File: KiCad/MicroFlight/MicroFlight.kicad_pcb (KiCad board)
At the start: 2 copper layers, 38 x 17 mm, 65 parts, among them J1 C2CK, J10 SRV3, J2 C2D, J3 A, J4 B, J5 C, J6 BIND, J7 BAT, J8 SRV1, J9 SRV2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

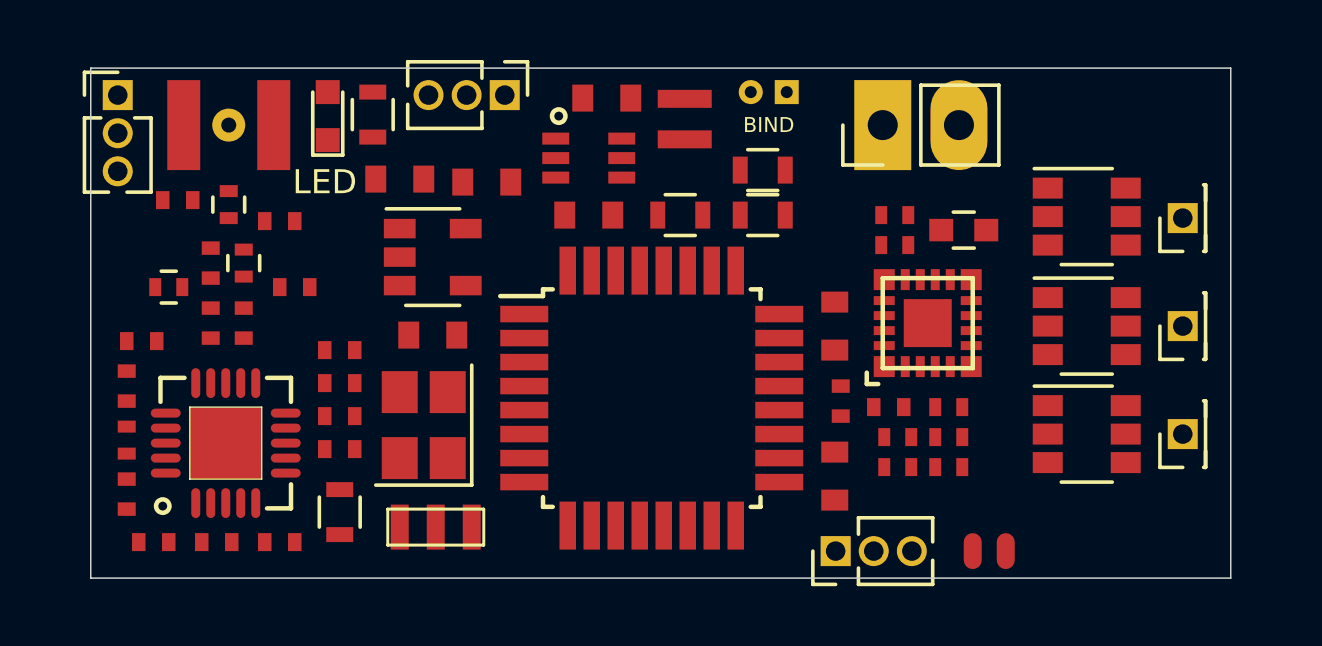
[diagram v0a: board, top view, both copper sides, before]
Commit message: PCB - added optional shunt for current sensing
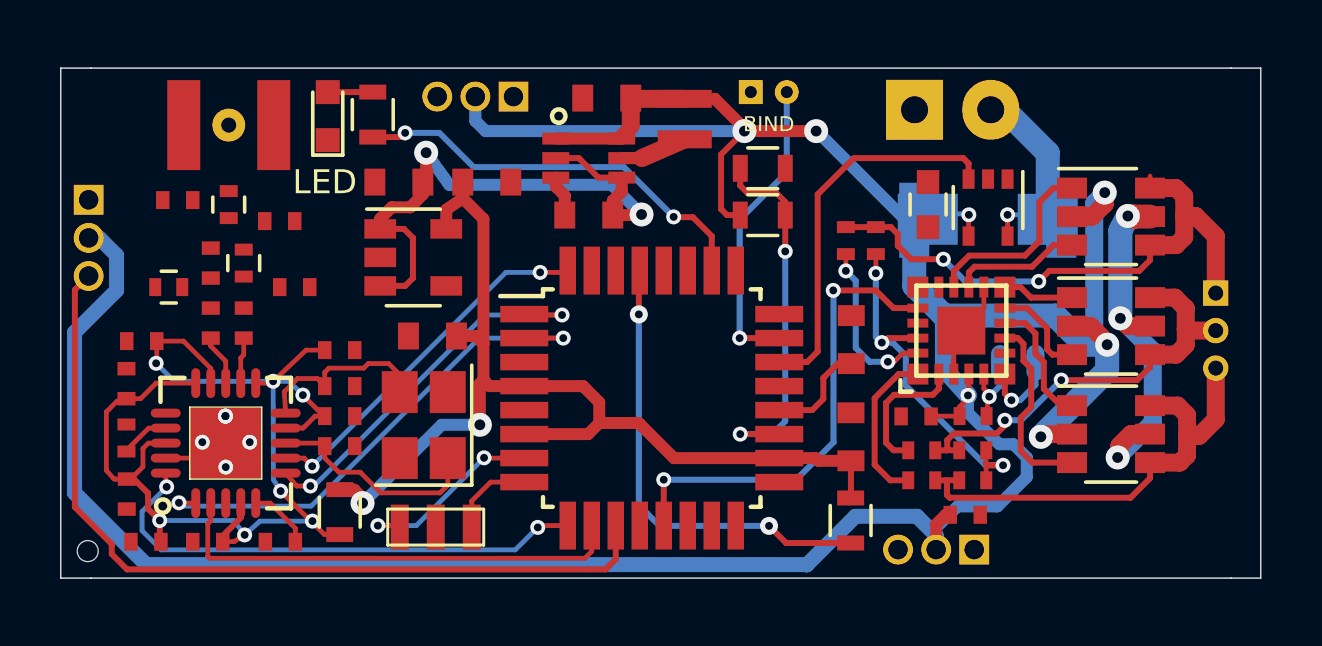
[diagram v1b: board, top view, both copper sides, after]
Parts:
- removed J4: B, Pin_Headers:Pin_Header_Straight_1x01_Pitch1.27mm
- removed J5: C, Pin_Headers:Pin_Header_Straight_1x01_Pitch1.27mm
- added R13: 0.022, Resistors_SMD:R_1206_HandSoldering, B.Cu at (126.9, 85.5)
- added R14: 0.022, Resistors_SMD:R_2010, B.Cu at (126.9, 85.6)
- added REF**: hole, KiCadCustomLibs:hole_0.7, F.Cu at (96.9, 96.6)
- added U6: MAX9610, TO_SOT_Packages_SMD:SOT-353_SC-70-5, F.Cu at (126.9, 85.2)
- J1, J10, J2, J8, J9: moved to B.Cu
- J3: value A -> MOTOR; footprint Pin_Headers:Pin_Header_Straight_1x01_Pitch1.27mm -> Connectors_Molex:Molex_PicoBlade_53047-0310_03x1.25mm_Straight; moved to B.Cu
- moved R4 11.7 mm to (122.3, 95.6), turned to 270 degrees
- moved J2 6.36 mm to (128.5, 90.3), turned to 90 degrees
- moved J1 6.34 mm to (127.3, 90.3), turned to 270 degrees
- moved C26 5.62 mm to (126.2, 95.4), turned to 180 degrees
- moved C7 5.34 mm to (108.4, 89.4)
- moved C5 5.22 mm to (107.3, 84.3), turned to 180 degrees
- moved J10 4.62 mm to (126.5, 96.5)
- moved J8 3.62 mm to (96.9, 84.9), turned to 180 degrees
- moved J3 2.73 mm to (134.5, 88.0), turned to 270 degrees
- moved C9 2.40 mm to (100.9, 96.3)
- moved C10 2.12 mm to (103.3, 96.3)
- moved R8 1.64 mm to (122.2, 86.2), turned to 270 degrees
- moved C24 1.46 mm to (124.9, 85.0), turned to 270 degrees
- moved C4 1.42 mm to (122.3, 92.8), turned to 90 degrees
- moved J7 1.18 mm to (124.5, 81.9)
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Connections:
- J7 pad 2: +BATT -> Net-(J7-Pad2)
- R1 pad 1: /A2 -> /A1
- R2 pad 2: /A2 -> /A1
- U2 pad 19: Net-(U2-Pad19) -> /A1
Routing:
- net +BATT: track 0.00 -> 110.6 mm, vias 0 -> 7
- net VCC: track 0.00 -> 39.1 mm, vias 0 -> 7
- net +3V3: track 0.00 -> 34.6 mm, vias 0 -> 2
- net /CH1: track 0.00 -> 28.2 mm
- net GND: track 0.00 -> 28.2 mm, vias 0 -> 8
- net /5V: track 0.00 -> 20.2 mm, vias 0 -> 2
- net /uESC1S/M_A: track 0.00 -> 19.4 mm, vias 0 -> 2
- net /SI: track 0.00 -> 17.1 mm, vias 0 -> 2
- net /SCLK: track 0.00 -> 17.0 mm, vias 0 -> 2
- net /uESC1S/M_C: track 0.00 -> 16.6 mm
- net /CH3: track 0.00 -> 15.8 mm, vias 0 -> 2
- net /SO: track 0.00 -> 15.6 mm
- net Net-(R4-Pad2): track 0.00 -> 15.4 mm, vias 0 -> 2
- net /uESC1S/M_B: track 0.00 -> 14.3 mm, vias 0 -> 2
- net Net-(R3-Pad2): track 0.00 -> 13.9 mm, vias 0 -> 2
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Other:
- board size 38 x 17 mm -> 40 x 17 mm
- net class Default: clearance 0.2 -> 0.16; trace_width 0.25 -> 0.16; via_dia 0.8 -> 0.5; via_drill 0.4 -> 0.26
- net class PWR added: clearance 0.2, trace_width 0.6, via_dia 0.8, via_drill 0.36
- rule solder_mask_min_width: 0.25 -> 0.1
- rule trace_clearance: 0.2 -> 0.16
- rule trace_min: 0.2 -> 0.16
- rule via_min_drill: 0.3 -> 0.26
